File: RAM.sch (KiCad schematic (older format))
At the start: 3 parts, among them U7 IS61C5128AL-10KLI

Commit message: Fix BOM swap of 1u and 4.7u caps
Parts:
- C28, C29: Mouser 187-CL10A475KP8NNNC -> 810-CGA3E1X7R1C105AC
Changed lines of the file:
@@
 F 2 "Passive:CAPC1608X100" H 7200 3900 50  0001 C CNN
 F 3 "~" H 7200 3900 50  0001 C CNN
-F 4 "187-CL10A475KP8NNNC" H 0   0   50  0001 C CNN "Mouser"
+F 4 "810-CGA3E1X7R1C105AC" H 0   0   50  0001 C CNN "Mouser"
 	1    7200 3900
 	1    0    0    -1
@@
 F 2 "Passive:CAPC1608X100" H 7450 3900 50  0001 C CNN
 F 3 "~" H 7450 3900 50  0001 C CNN
-F 4 "187-CL10A475KP8NNNC" H 0   0   50  0001 C CNN "Mouser"
+F 4 "810-CGA3E1X7R1C105AC" H 0   0   50  0001 C CNN "Mouser"
 	1    7450 3900
 	1    0    0    -1

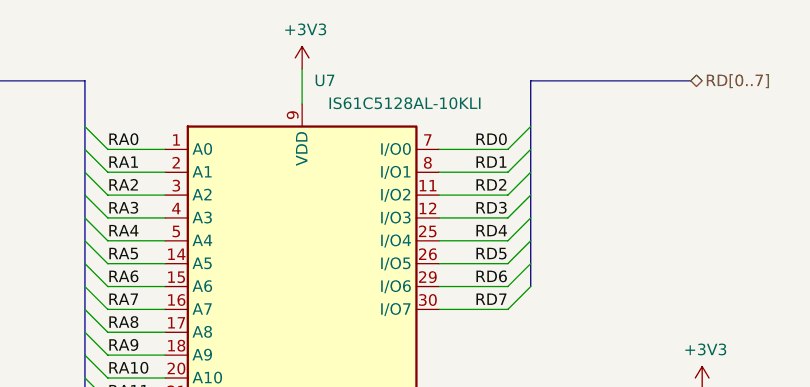
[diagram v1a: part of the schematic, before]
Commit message: Fix SRAM manufacturer part number
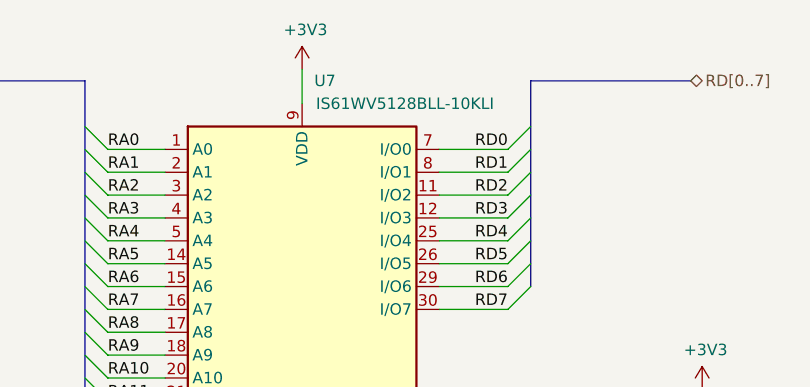
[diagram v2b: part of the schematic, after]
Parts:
- U7: value IS61C5128AL-10KLI -> IS61WV5128BLL-10KLI
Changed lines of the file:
@@
 AR Path="/603A03FF/603A5B22" Ref="U7"  Part="1"
 F 0 "U7" H 5800 5100 50  0000 C CNN
-F 1 "IS61C5128AL-10KLI" H 6150 5000 50  0000 C CNN
+F 1 "IS61WV5128BLL-10KLI" H 6150 5000 50  0000 C CNN
 F 2 "Active:SOJ127P1118X376-36" H 5200 4850 50  0001 C CNN
 F 3 "https://www.mouser.com/datasheet/2/198/61-64WV5128Axx-Bxx-258353.pdf" H 5700 3700 50  0001 C CNN
